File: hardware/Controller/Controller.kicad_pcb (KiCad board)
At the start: 2 copper layers, 103.3 x 39.9 mm, 36 parts, among them J1 GPIO, J2 Conn_02x11_Counter_Clockwise, J3 ICSP Header, J7 UART DEBUG, Q2 NMOS, SW1 Button - User Interface, SW2 Button - Reset, U1 CAT24C256, U4 ATmega328-P, Y2 16 Mhz

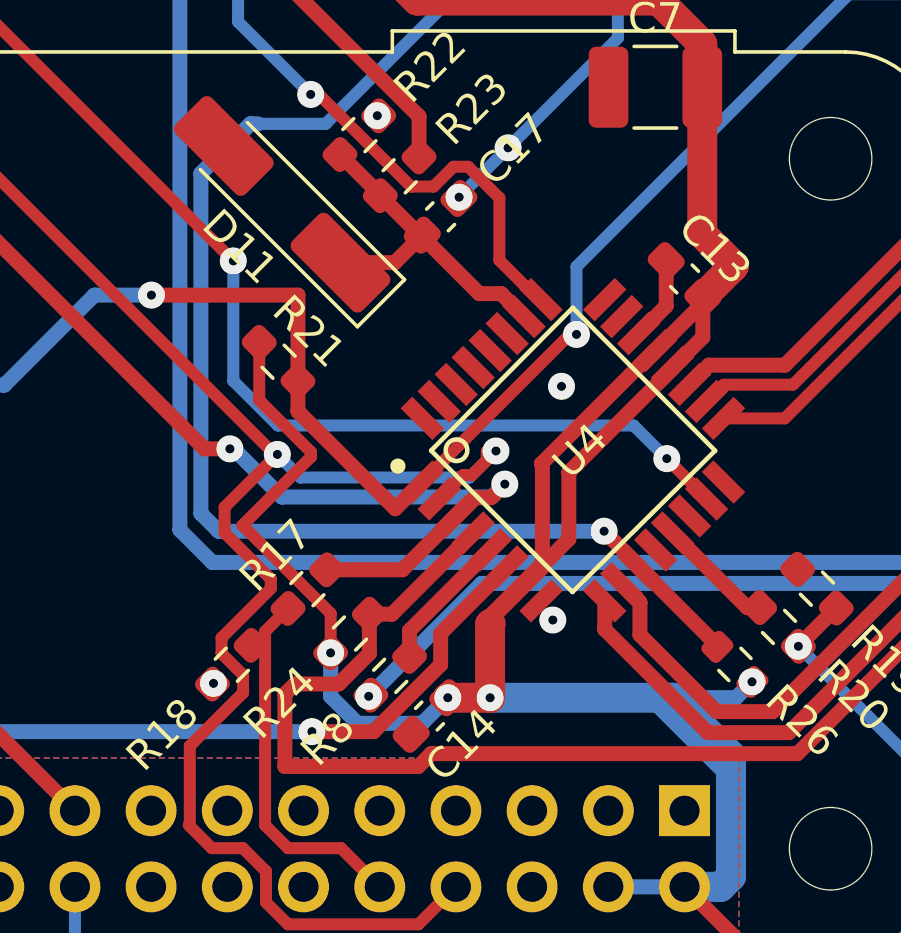
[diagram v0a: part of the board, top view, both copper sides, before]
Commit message: Hardware cleanup & enclosure prototype
* Seperates the kicad project into seperate projects per PCB
* initial FreeCAD Assets and prototypes added
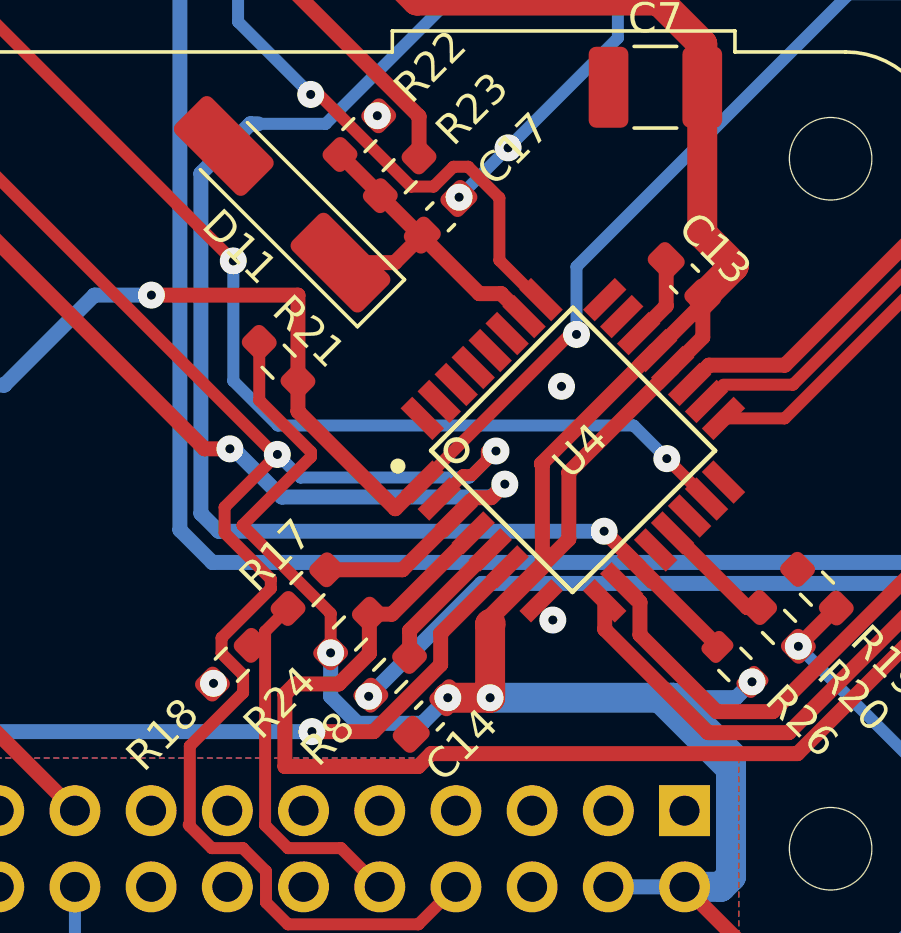
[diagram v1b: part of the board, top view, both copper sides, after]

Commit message: Hardware - Controller - Rev 0.3
* Consolidate various asset dirs into single symlinked directory.
* Fixes major flaw with previous atmega328 layout - wrong schematic symbol caused incorrect routing
* Use smaller crystal closer to mcu
* Add QR to silkscreen
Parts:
- removed U4: ATmega328-P, ATMEGA328-AU:QFP80P900X900X120-32N
- removed Y2: 16 Mhz, Crystal - 16MHz ECS_160_20_5PX_TR:XTAL_ECS-160-20-5PX-TR
- added U2: ATmega328P-A, Package_QFP:TQFP-32_7x7mm_P0.8mm, F.Cu at (167.6, 169.1)
- added Y1: ECS-160-20-33-TR, ECS-160-20-33-TR:XTAL_ECS-160-20-33-TR, F.Cu at (164.4, 177.0)
- C7: value 47uF 1210 -> 47uF
- D11: footprint Diode_SMD:D_MiniMELF_Handsoldering -> Diode_SMD:D_SOD-323_HandSoldering
- Q2: value NMOS -> AOSP36326C; footprint FET - AOSP36326C:SOIC127P490X600X175-8N -> AOSP36326C:SOIC127P490X600X175-8N
- SW1, SW2: footprint Button - PTS815 Tactile SW:SW4_PTS815 SJM 250 SMTR LFS_CNK -> Button - PTS815:SW4_PTS815 SJM 250 SMTR LFS_CNK
- U1: footprint CAT24C256WI-GT3:SOIC127P600X175-8N -> IC - CAT24C256WI-GT3:SOIC127P600X175-8N
- moved C15 38.1 mm to (162.8, 175.0), turned to -135 degrees
- moved C16 28.3 mm to (166.3, 179.5), turned to 45 degrees
- moved R24 18.2 mm to (155.4, 166.6), turned to -45 degrees
- moved R18 16.9 mm to (157.6, 164.3), turned to -45 degrees
- moved R17 16.1 mm to (156.5, 165.4), turned to 135 degrees
- moved R8 14.4 mm to (159.0, 171.4)
- moved C14 13.6 mm to (161.0, 173.2)
- moved R19 10.8 mm to (174.3, 175.3)
- moved R20 10.7 mm to (173.1, 176.5)
- moved G*** 10.3 mm to (196.3, 171.1)
- moved R26 10.3 mm to (172.1, 177.7)
- moved R21 10.3 mm to (158.8, 163.2)
- moved C17 10.1 mm to (164.1, 158.8), turned to -45 degrees
- moved R23 9.48 mm to (161.8, 161.1), turned to 135 degrees
- moved C13 7.97 mm to (172.8, 164.8)
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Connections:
- J3 pad 2: /Power State/SCK -> +5V
- J3 pad 3: /Power State/Reset -> /Power State/SCK
- J3 pad 4: GND -> /Power State/MOSI
- J3 pad 5: /Power State/MOSI -> /Power State/Reset
- J3 pad 6: +5V -> GND
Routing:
- net /GPIO15/RXD0: track 12.2 -> 60.7 mm, vias 0 -> 1
- net GND: track 47.5 -> 9.96 mm, vias 6 -> 51
- net Net-(U2-XTAL1/PB6): track 33.8 -> 4.36 mm
- net Rx: track 61.5 -> 83.7 mm
- net /GPIO24: track 46.1 -> 24.9 mm
- net +5V: track 179.5 -> 158.7 mm
- net Tx: track 45.9 -> 26.6 mm, vias 2 -> 1
- net Net-(U2-XTAL2/PB7): track 25.4 -> 7.58 mm
- net /Power State/Pi_En: track 50.4 -> 33.3 mm
- net Net-(D10-DIN): track 44.3 -> 60.6 mm
- net Button: track 66.3 -> 82.3 mm, vias 0 -> 3
- net Chrg_Stat: track 46.6 -> 35.7 mm, vias 1 -> 2
- net /Power State/Reset: track 89.5 -> 78.6 mm
- net /Power State/MOSI: track 25.5 -> 35.3 mm, vias 0 -> 1
- net /Power State/SCK: track 20.1 -> 28.3 mm, vias 0 -> 1
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- added copper zone on F.Cu, net +5V
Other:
- board text added: "+5V"
- board text added: "5V!"
- board text added: "GND"
- board text added: "MI"
- board text added: "MO"
- board text added: "RST"
- board text added: "RX"
- board text added: "Rev 0.4 - 2025 - KBader94 https://github.com/kbader94/OpenActionCam"
- board text added: "SCK"
- board text added: "Status"
- board text added: "TX"
- board text removed: "UART 5V"
- board text removed: "V 0.2 - 2025 - KBader94 https://github.com/kbader94/OpenActionCam"
